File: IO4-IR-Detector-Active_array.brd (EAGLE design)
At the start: 107.6 x 107.6 mm, 124 parts, among them Q1X11 NPN-2222, Q1X12 NPN-2222, Q1X21 NPN-2222, Q1X22 NPN-2222, Q2X11 NPN-2222, Q2X12 NPN-2222, Q2X21 NPN-2222, Q2X22 NPN-2222, Q3X11 NPN-2222, Q3X12 NPN-2222, Q3X21 NPN-2222, Q3X22 NPN-2222, Q4X11 NPN-2222, Q4X12 NPN-2222, Q4X21 NPN-2222, Q4X22 NPN-2222

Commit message: added values for connectors
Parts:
- CON1X11, CON1X12, CON1X21, CON1X22: value (none) -> RJ12/6
- JP1X11, JP1X12, JP1X21, JP1X22, JP2X11, JP2X12, JP2X21, JP2X22, JP3X11, JP3X12, JP3X21, JP3X22, JP4X11, JP4X12, JP4X21, JP4X22: value (none) -> 0.100
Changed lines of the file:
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@@
 <setting verticaltext="up"/>
 </settings>
-<grid distance="1" unitdist="mm" unit="mm" style="dots" multiple="2" display="yes" altdistance="0.5" altunitdist="mm" altunit="mm"/>
+<grid distance="50" unitdist="mil" unit="mil" style="dots" multiple="2" display="yes" altdistance="25" altunitdist="mil" altunit="mil"/>
 <layers>
 <layer number="1" name="Top" color="4" fill="1" visible="yes" active="yes"/>
@@
 <element name="C2X11" library="SPCoast" package="0805-CAP" value="0.1uF" x="15.24" y="41.91" rot="R90"/>
 <element name="C3X11" library="SPCoast" package="0810-CAP" value="220uF" x="38.608" y="4.826"/>
-<element name="CON1X11" library="SPCoast" package="RJ25-PANEL" value="" x="22.86" y="3.175"/>
-<element name="JP1X11" library="SPCoast" package="1X04_LOCK" value="" x="42.545" y="41.91" rot="R180"/>
-<element name="JP2X11" library="SPCoast" package="1X04_LOCK" value="" x="42.545" y="31.75" rot="R180"/>
-<element name="JP3X11" library="SPCoast" package="1X04_LOCK" value="" x="42.545" y="21.59" rot="R180"/>
-<element name="JP4X11" library="SPCoast" package="1X04_LOCK" value="" x="42.545" y="11.43" rot="R180"/>
+<element name="CON1X11" library="SPCoast" package="RJ25-PANEL" value="RJ12/6" x="22.86" y="3.175"/>
+<element name="JP1X11" library="SPCoast" package="1X04_LOCK" value="0.100" x="42.545" y="41.91" rot="R180"/>
+<element name="JP2X11" library="SPCoast" package="1X04_LOCK" value="0.100" x="42.545" y="31.75" rot="R180"/>
+<element name="JP3X11" library="SPCoast" package="1X04_LOCK" value="0.100" x="42.545" y="21.59" rot="R180"/>
+<element name="JP4X11" library="SPCoast" package="1X04_LOCK" value="0.100" x="42.545" y="11.43" rot="R180"/>
 <element name="LED1X11" library="SPCoast" package="0603-LED" value="Y" x="13.97" y="3.81" rot="R270"/>
 <element name="LED2X11" library="SPCoast" package="0603-LED" value="Y" x="11.43" y="3.81" rot="R270"/>
@@
 <element name="C2X12" library="SPCoast" package="0805-CAP" value="0.1uF" x="15.24" y="91.91" rot="R90"/>
 <element name="C3X12" library="SPCoast" package="0810-CAP" value="220uF" x="38.608" y="54.826"/>
-<element name="CON1X12" library="SPCoast" package="RJ25-PANEL" value="" x="22.86" y="53.175"/>
-<element name="JP1X12" library="SPCoast" package="1X04_LOCK" value="" x="42.545" y="91.91" rot="R180"/>
-<element name="JP2X12" library="SPCoast" package="1X04_LOCK" value="" x="42.545" y="81.75" rot="R180"/>
-<element name="JP3X12" library="SPCoast" package="1X04_LOCK" value="" x="42.545" y="71.59" rot="R180"/>
-<element name="JP4X12" library="SPCoast" package="1X04_LOCK" value="" x="42.545" y="61.43" rot="R180"/>
+<element name="CON1X12" library="SPCoast" package="RJ25-PANEL" value="RJ12/6" x="22.86" y="53.175"/>
+<element name="JP1X12" library="SPCoast" package="1X04_LOCK" value="0.100" x="42.545" y="91.91" rot="R180"/>
+<element name="JP2X12" library="SPCoast" package="1X04_LOCK" value="0.100" x="42.545" y="81.75" rot="R180"/>
+<element name="JP3X12" library="SPCoast" package="1X04_LOCK" value="0.100" x="42.545" y="71.59" rot="R180"/>
+<element name="JP4X12" library="SPCoast" package="1X04_LOCK" value="0.100" x="42.545" y="61.43" rot="R180"/>
 <element name="LED1X12" library="SPCoast" package="0603-LED" value="Y" x="13.97" y="53.81" rot="R270"/>
 <element name="LED2X12" library="SPCoast" package="0603-LED" value="Y" x="11.43" y="53.81" rot="R270"/>
@@
 <element name="C2X21" library="SPCoast" package="0805-CAP" value="0.1uF" x="65.24" y="41.91" rot="R90"/>
 <element name="C3X21" library="SPCoast" package="0810-CAP" value="220uF" x="88.608" y="4.826"/>
-<element name="CON1X21" library="SPCoast" package="RJ25-PANEL" value="" x="72.86" y="3.175"/>
-<element name="JP1X21" library="SPCoast" package="1X04_LOCK" value="" x="92.545" y="41.91" rot="R180"/>
-<element name="JP2X21" library="SPCoast" package="1X04_LOCK" value="" x="92.545" y="31.75" rot="R180"/>
-<element name="JP3X21" library="SPCoast" package="1X04_LOCK" value="" x="92.545" y="21.59" rot="R180"/>
-<element name="JP4X21" library="SPCoast" package="1X04_LOCK" value="" x="92.545" y="11.43" rot="R180"/>
+<element name="CON1X21" library="SPCoast" package="RJ25-PANEL" value="RJ12/6" x="72.86" y="3.175"/>
+<element name="JP1X21" library="SPCoast" package="1X04_LOCK" value="0.100" x="92.545" y="41.91" rot="R180"/>
+<element name="JP2X21" library="SPCoast" package="1X04_LOCK" value="0.100" x="92.545" y="31.75" rot="R180"/>
+<element name="JP3X21" library="SPCoast" package="1X04_LOCK" value="0.100" x="92.545" y="21.59" rot="R180"/>
+<element name="JP4X21" library="SPCoast" package="1X04_LOCK" value="0.100" x="92.545" y="11.43" rot="R180"/>
 <element name="LED1X21" library="SPCoast" package="0603-LED" value="Y" x="63.97" y="3.81" rot="R270"/>
 <element name="LED2X21" library="SPCoast" package="0603-LED" value="Y" x="61.43" y="3.81" rot="R270"/>
@@
 <element name="C2X22" library="SPCoast" package="0805-CAP" value="0.1uF" x="65.24" y="91.91" rot="R90"/>
 <element name="C3X22" library="SPCoast" package="0810-CAP" value="220uF" x="88.608" y="54.826"/>
-<element name="CON1X22" library="SPCoast" package="RJ25-PANEL" value="" x="72.86" y="53.175"/>
-<element name="JP1X22" library="SPCoast" package="1X04_LOCK" value="" x="92.545" y="91.91" rot="R180"/>
-<element name="JP2X22" library="SPCoast" package="1X04_LOCK" value="" x="92.545" y="81.75" rot="R180"/>
-<element name="JP3X22" library="SPCoast" package="1X04_LOCK" value="" x="92.545" y="71.59" rot="R180"/>
-<element name="JP4X22" library="SPCoast" package="1X04_LOCK" value="" x="92.545" y="61.43" rot="R180"/>
+<element name="CON1X22" library="SPCoast" package="RJ25-PANEL" value="RJ12/6" x="72.86" y="53.175"/>
+<element name="JP1X22" library="SPCoast" package="1X04_LOCK" value="0.100" x="92.545" y="91.91" rot="R180"/>
+<element name="JP2X22" library="SPCoast" package="1X04_LOCK" value="0.100" x="92.545" y="81.75" rot="R180"/>
+<element name="JP3X22" library="SPCoast" package="1X04_LOCK" value="0.100" x="92.545" y="71.59" rot="R180"/>
+<element name="JP4X22" library="SPCoast" package="1X04_LOCK" value="0.100" x="92.545" y="61.43" rot="R180"/>
 <element name="LED1X22" library="SPCoast" package="0603-LED" value="Y" x="63.97" y="53.81" rot="R270"/>
 <element name="LED2X22" library="SPCoast" package="0603-LED" value="Y" x="61.43" y="53.81" rot="R270"/>

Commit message: normalized values
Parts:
- ARDUINO1X11, ARDUINO1X12, ARDUINO1X21, ARDUINO1X22: value ARDUINO-PRO-MINIDAVESROBOT -> DAVEK
- C1X11, C1X12, C1X21, C1X22, C2X11, C2X12, C2X21, C2X22: device SPCoast:0805-CAP -> SPCoast:0603-CAP
- R10X11, R10X12, R10X21, R11X11, R11X12, R11X21, R12X11, R12X12, R12X21, R14X11, R14X12, R14X21, R1X11, R1X12, R1X21, R2X11, R2X12, R2X21, R3X11, R3X12, R3X21, R4X11, R4X12, R4X21, R5X11, R5X12, R5X21, R6X11, R6X12, R6X21, R7X11, R7X12, R7X21, R8X11, R8X12, R8X21, R9X11, R9X12, R9X21: device SPCoast:0805-RES -> SPCoast:0603-RES

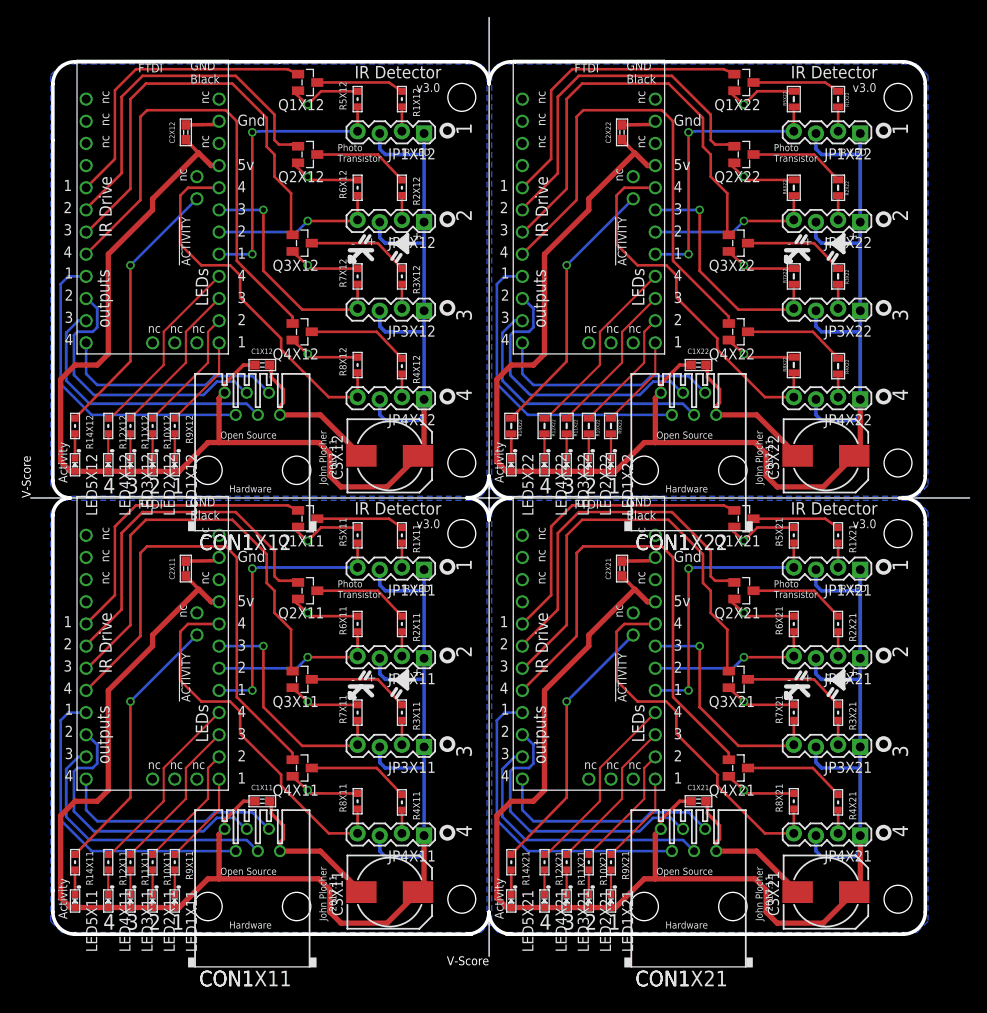
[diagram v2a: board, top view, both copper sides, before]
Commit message: make room for conveyer fingers
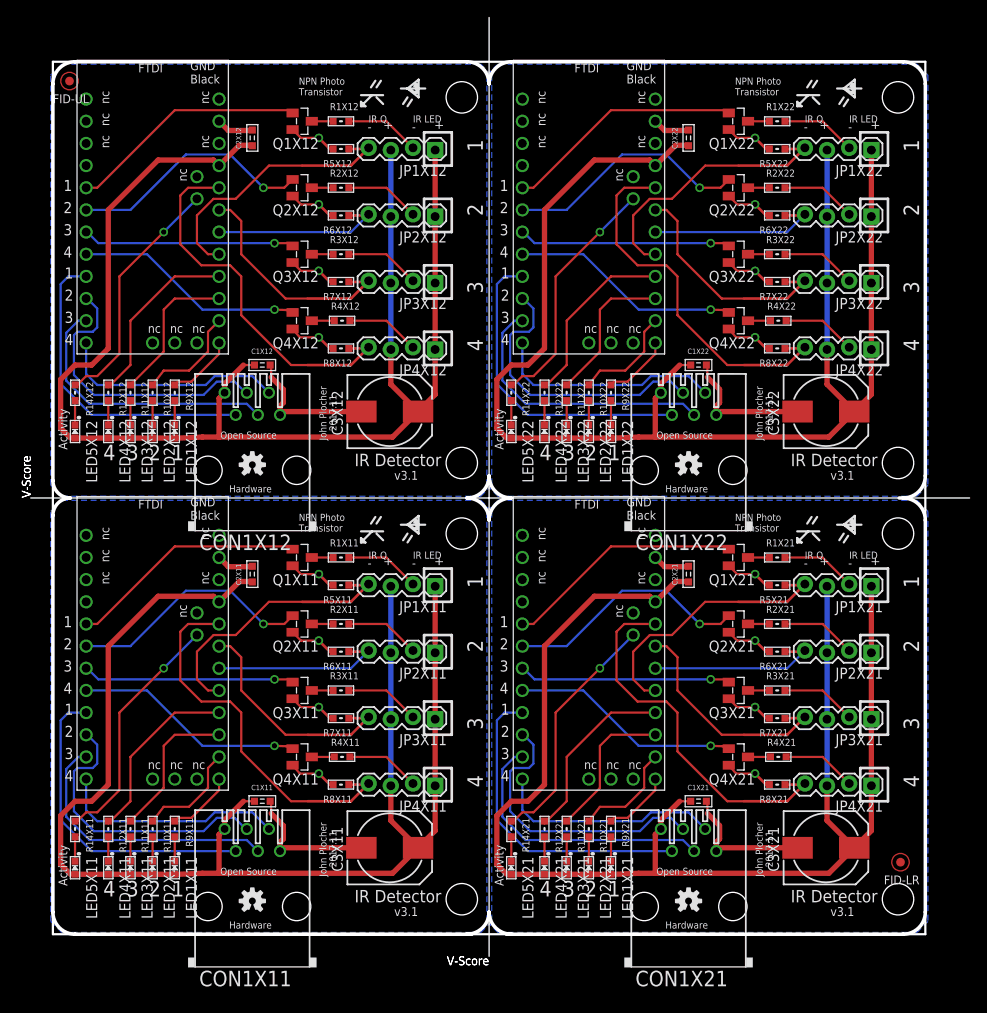
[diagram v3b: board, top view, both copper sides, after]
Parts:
- added FID-LR, FID-UL: (no value), SPCoast:FIDUCIAL_1MM
- added OSH_LOGOX11, OSH_LOGOX12, OSH_LOGOX21, OSH_LOGOX22: DOC-OSHW-LOGO-S, SPCoast:OSHW-LOGO-S
- R10X22, R11X22, R12X22, R5X22, R6X22, R7X22, R8X22, R9X22: device SPCoast:0805-RES -> SPCoast:0603-RES
- R14X11, R14X12, R14X21: value 2k0 -> 5k0
- R14X22: value 2k0 -> 5k0; device SPCoast:0805-RES -> SPCoast:0603-RES
- R1X11, R1X12, R1X21, R2X11, R2X12, R2X21, R3X11, R3X12, R3X21, R4X11, R4X12, R4X21: value 1k0 -> 330R
- R1X22, R2X22, R3X22, R4X22: value 1k0 -> 330R; device SPCoast:0805-RES -> SPCoast:0603-RES
- moved R4X11 8.61 mm to (33.1, 20.3), turned to 0 degrees
- moved R4X12 8.61 mm to (33.1, 70.3), turned to 0 degrees
- moved R4X21 8.61 mm to (83.1, 20.3), turned to 0 degrees
- moved R4X22 8.61 mm to (83.1, 70.3), turned to 0 degrees
- moved C2X21 7.65 mm to (72.9, 41.3)
- moved C2X22 7.65 mm to (72.9, 91.3)
- moved C2X11 7.65 mm to (22.9, 41.3)
- moved C2X12 7.65 mm to (22.9, 91.3)
- moved R1X11 7.43 mm to (33.0, 43.2), turned to 0 degrees
- moved R1X21 7.43 mm to (83.0, 43.2), turned to 0 degrees
- moved R3X11 7.43 mm to (33.0, 27.9), turned to 0 degrees
- moved R3X21 7.43 mm to (83.0, 27.9), turned to 0 degrees
- moved R1X12 7.43 mm to (33.0, 93.2), turned to 0 degrees
- moved R1X22 7.43 mm to (83.0, 93.2), turned to 0 degrees
- moved R3X12 7.43 mm to (33.0, 77.9), turned to 0 degrees
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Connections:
- net V+X11 renamed VCCX11
- net V+X12 renamed VCCX12
- net V+X21 renamed VCCX21
- net V+X22 renamed VCCX22
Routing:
- net IR4X22: track 56.0 -> 26.3 mm, vias 0 -> 1
- net IR4X12: track 56.0 -> 26.3 mm, vias 0 -> 1
- net IR4X11: track 56.0 -> 26.3 mm, vias 0 -> 1
- net IR4X21: track 56.0 -> 26.3 mm, vias 0 -> 1
- net IR3X12: track 50.0 -> 24.4 mm, vias 0 -> 1
- net IR3X22: track 50.0 -> 24.4 mm, vias 0 -> 1
- net IR3X11: track 50.0 -> 24.4 mm, vias 0 -> 1
- net IR3X21: track 50.0 -> 24.4 mm, vias 0 -> 1
- net IR2X21: track 40.9 -> 28.3 mm, vias 0 -> 1
- net IR2X11: track 40.9 -> 28.3 mm, vias 0 -> 1
- net IR2X22: track 40.9 -> 28.3 mm, vias 0 -> 1
- net IR2X12: track 40.9 -> 28.3 mm, vias 0 -> 1
- net VCCX21: track 175.8 -> 163.9 mm
- net VCCX12: track 175.8 -> 163.9 mm
- net VCCX11: track 175.8 -> 163.9 mm
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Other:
- outline, holes or cut-outs redrawn
- board text added: "#1"
- board text added: "#2"
- board text added: "#3"
- board text added: "#4"
- board text added: "+5v"
- board text added: "Auto compensates for changes in ambient light"
- board text added: "GND"
- board text added: "IR Detector - Active"
- board text added: "IR Q"
- board text added: "Infrared Emitter IR 940nm"
- board text added: "Infrared Emitters IR 940nm"
- board text added: "NPN Photo Transistor"
- board text added: "v3.1"
- board text removed: "!ACTIVITY"
- board text removed: "5v"
- board text removed: "Auto compensates for ambient light"
- board text removed: "Gnd"
- board text removed: "IR Drive"
- board text removed: "Infrared Emitters IR 940nm 34 deg Water Clear"
- board text removed: "LEDs"
- board text removed: "Photo Transistor"
- board text removed: "Solder Side"
- board text removed: "outputs"
- board text removed: "v3.0"
